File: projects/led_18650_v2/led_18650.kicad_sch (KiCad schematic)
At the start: 3 parts

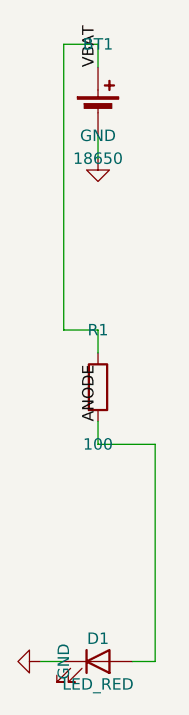
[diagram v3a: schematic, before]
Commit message: Phase 3: parametric cluster wiring generators (internal/place2/wiregen)
Closed-form wiring (straight or single-L with clear-corridor
preconditions) for decoupling, 2-pin satellites, dividers and crystal
load caps; generators apply or decline, never search. Integrated as a
pre-pass in connect_netlist with component-aware MST; discovery-label
fallback now also fires for nets fully consumed by wiregen (fixes
dropped-net regression, covered by two regression tests).

Co-Authored-By: Claude Fable 5 <noreply@anthropic.com>
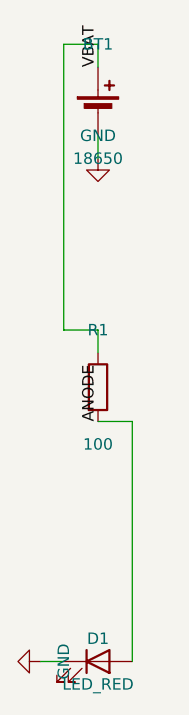
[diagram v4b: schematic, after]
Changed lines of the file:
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@@
     (instances
       (project ""
-        (path "/94f060c2-a7f5-4c45-a07d-df6b788d50ea" (reference "BT1") (unit 1)))))
+        (path "/788d7bce-e481-48d8-802d-65b6fb32a004" (reference "BT1") (unit 1)))))
   (symbol (lib_id "Device:R")
     (at 50.8 81.28 0) (unit 1) (exclude_from_sim no) (in_bom yes) (on_board yes) (dnp no)
@@
     (instances
       (project ""
-        (path "/94f060c2-a7f5-4c45-a07d-df6b788d50ea" (reference "R1") (unit 1)))))
+        (path "/788d7bce-e481-48d8-802d-65b6fb32a004" (reference "R1") (unit 1)))))
   (symbol (lib_id "Device:LED")
     (at 50.8 111.76 0) (unit 1) (exclude_from_sim no) (in_bom yes) (on_board yes) (dnp no)
@@
     (instances
       (project ""
-        (path "/94f060c2-a7f5-4c45-a07d-df6b788d50ea" (reference "D1") (unit 1)))))
+        (path "/788d7bce-e481-48d8-802d-65b6fb32a004" (reference "D1") (unit 1)))))
+  (wire
+    (pts (xy 54.61 111.76) (xy 54.61 85.09))
+    (stroke (width 0) (type default)))
+  (wire
+    (pts (xy 54.61 85.09) (xy 50.8 85.09))
+    (stroke (width 0) (type default)))
   (wire
     (pts (xy 50.8 45.72) (xy 50.8 43.18))
@@
       (effects
         (font (size 1.27 1.27)) (hide yes))))
-  (wire
-    (pts (xy 50.8 85.09) (xy 50.8 87.63))
-    (stroke (width 0) (type default)))
-  (wire
-    (pts (xy 50.8 87.63) (xy 57.15 87.63))
-    (stroke (width 0) (type default)))
-  (wire
-    (pts (xy 57.15 87.63) (xy 57.15 111.76))
-    (stroke (width 0) (type default)))
-  (wire
-    (pts (xy 57.15 111.76) (xy 54.61 111.76))
-    (stroke (width 0) (type default)))
   (label "ANODE"
     (at 50.8 85.09 270) (fields_autoplaced yes)
@@
     (instances
       (project ""
-        (path "/94f060c2-a7f5-4c45-a07d-df6b788d50ea" (reference "#PWR01") (unit 1)))))
+        (path "/788d7bce-e481-48d8-802d-65b6fb32a004" (reference "#PWR01") (unit 1)))))
   (wire
     (pts (xy 46.99 111.76) (xy 44.45 111.76))
@@
     (instances
       (project ""
-        (path "/94f060c2-a7f5-4c45-a07d-df6b788d50ea" (reference "#PWR02") (unit 1)))))
+        (path "/788d7bce-e481-48d8-802d-65b6fb32a004" (reference "#PWR02") (unit 1)))))
   (wire
     (pts (xy 50.8 53.34) (xy 50.8 55.88))

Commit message: Phase 4: per-pin power rail policy + full pipeline determinism
Power nets are never routed: every pin on a rail gets its own power
symbol (GND down, VCC up) with a 2.54mm stub; PWR_FLAG emitted after
the gate for undriven power_in nets. Determinism: cluster detection
and TraceNets no longer depend on Go map iteration order (refOrder
slices, sorted canonical net naming). 6/6 identical runs on vreg and
mcu demos; vreg ERC now has zero errors.

Co-Authored-By: Claude Fable 5 <noreply@anthropic.com>
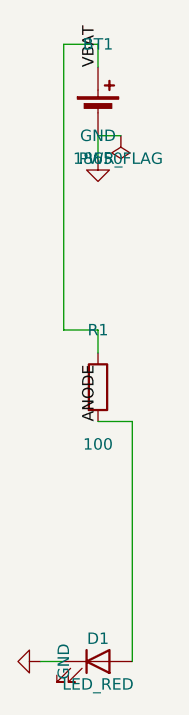
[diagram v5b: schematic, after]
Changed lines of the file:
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@@
     (instances
       (project ""
-        (path "/788d7bce-e481-48d8-802d-65b6fb32a004" (reference "BT1") (unit 1)))))
+        (path "/087d48b7-14f6-49e4-a252-8d3fa1ef42ce" (reference "BT1") (unit 1)))))
   (symbol (lib_id "Device:R")
     (at 50.8 81.28 0) (unit 1) (exclude_from_sim no) (in_bom yes) (on_board yes) (dnp no)
@@
     (instances
       (project ""
-        (path "/788d7bce-e481-48d8-802d-65b6fb32a004" (reference "R1") (unit 1)))))
+        (path "/087d48b7-14f6-49e4-a252-8d3fa1ef42ce" (reference "R1") (unit 1)))))
   (symbol (lib_id "Device:LED")
     (at 50.8 111.76 0) (unit 1) (exclude_from_sim no) (in_bom yes) (on_board yes) (dnp no)
@@
     (instances
       (project ""
-        (path "/788d7bce-e481-48d8-802d-65b6fb32a004" (reference "D1") (unit 1)))))
+        (path "/087d48b7-14f6-49e4-a252-8d3fa1ef42ce" (reference "D1") (unit 1)))))
   (wire
     (pts (xy 54.61 111.76) (xy 54.61 85.09))
@@
     (instances
       (project ""
-        (path "/788d7bce-e481-48d8-802d-65b6fb32a004" (reference "#PWR01") (unit 1)))))
+        (path "/087d48b7-14f6-49e4-a252-8d3fa1ef42ce" (reference "#PWR01") (unit 1)))))
   (wire
     (pts (xy 46.99 111.76) (xy 44.45 111.76))
@@
     (instances
       (project ""
-        (path "/788d7bce-e481-48d8-802d-65b6fb32a004" (reference "#PWR02") (unit 1)))))
+        (path "/087d48b7-14f6-49e4-a252-8d3fa1ef42ce" (reference "#PWR02") (unit 1)))))
   (wire
     (pts (xy 50.8 53.34) (xy 50.8 55.88))
+    (stroke (width 0) (type default)))
+  (symbol (lib_id "power:PWR_FLAG")
+    (at 53.34 53.34 180) (unit 1) (exclude_from_sim no) (in_bom no) (on_board no) (dnp no)
+    (property "Reference" "#FLG01"
+      (at 53.34 53.34 0)
+      (effects
+        (font (size 1.27 1.27)) (hide yes)))
+    (property "Value" "PWR_FLAG"
+      (at 53.34 55.88 0)
+      (effects
+        (font (size 1.27 1.27))))
+    (property "Footprint" ""
+      (at 53.34 53.34 0)
+      (effects
+        (font (size 1.27 1.27)) (hide yes)))
+    (property "Datasheet" ""
+      (at 53.34 53.34 0)
+      (effects
+        (font (size 1.27 1.27)) (hide yes)))
+    (property "Description" ""
+      (at 53.34 53.34 0)
+      (effects
+        (font (size 1.27 1.27)) (hide yes)))
+    (pin "1")
+    (instances
+      (project ""
+        (path "/087d48b7-14f6-49e4-a252-8d3fa1ef42ce" (reference "#FLG01") (unit 1)))))
+  (wire
+    (pts (xy 50.8 53.34) (xy 53.34 53.34))
     (stroke (width 0) (type default))))
